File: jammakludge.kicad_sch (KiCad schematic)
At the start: 22 parts, among them J1 Conn_02x28_Odd_Even, J2 Conn_02x28, J3 Conn_02x28

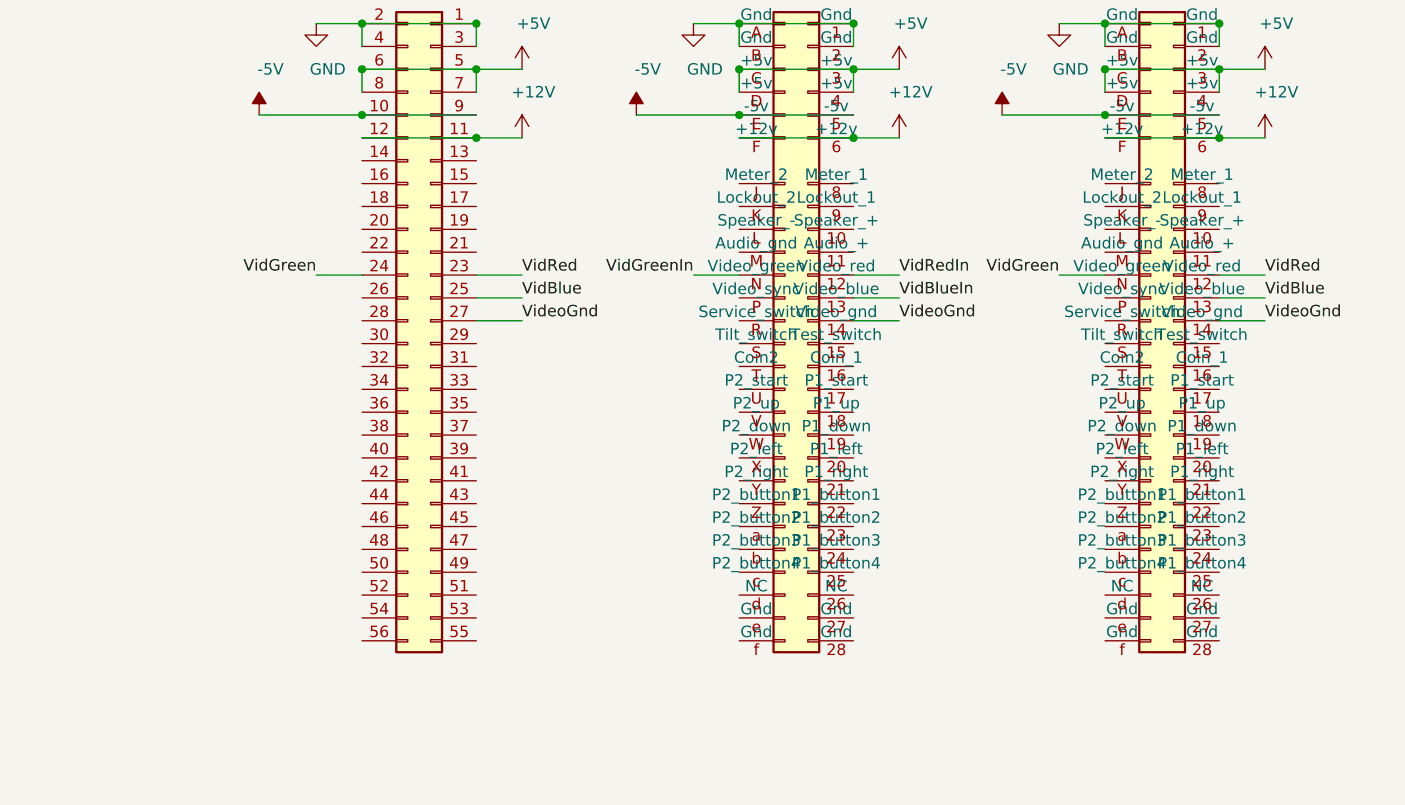
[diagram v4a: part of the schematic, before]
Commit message: labels added
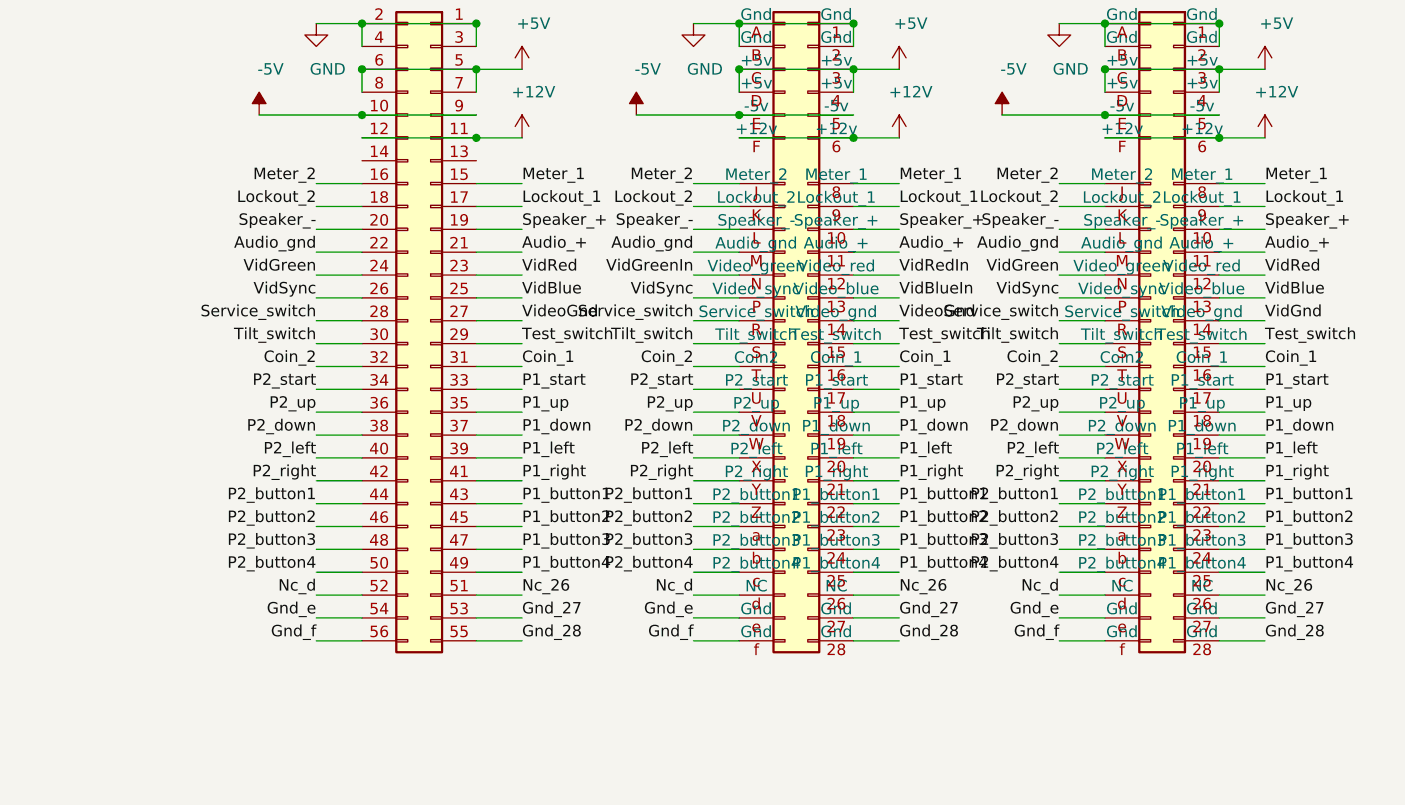
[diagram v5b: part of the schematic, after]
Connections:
- net VideoGnd: no longer J3.14 (Video_gnd)
- net Speaker_+: now reaches J3.10 (Speaker_+)
- net Speaker_+: now also J1.19 (Pin_19), J2.10 (Speaker_+)
- net Audio_+: now reaches J3.11 (Audio_+)
- net Audio_+: now also J1.21 (Pin_21), J2.11 (Audio_+)
- net Test_switch: now reaches J3.15 (Test_switch)
- net Test_switch: now also J1.29 (Pin_29), J2.15 (Test_switch)
- net Coin_1: now reaches J3.16 (Coin_1)
- net Coin_1: now also J1.31 (Pin_31), J2.16 (Coin_1)
- net P1_start: now reaches J3.17 (P1_start)
- net P1_start: now also J1.33 (Pin_33), J2.17 (P1_start)
- net P1_up: now reaches J3.18 (P1_up)
- net P1_up: now also J1.35 (Pin_35), J2.18 (P1_up)
- net P1_down: now reaches J3.19 (P1_down)
- net P1_down: now also J1.37 (Pin_37), J2.19 (P1_down)
- net P1_left: now reaches J3.20 (P1_left)
- net P1_left: now also J1.39 (Pin_39), J2.20 (P1_left)
- net P1_right: now reaches J3.21 (P1_right)
- net P1_right: now also J1.41 (Pin_41), J2.21 (P1_right)
- net P1_button1: now reaches J3.22 (P1_button1)
- net P1_button1: now also J1.43 (Pin_43), J2.22 (P1_button1)
- net P1_button2: now reaches J3.23 (P1_button2)
- net P1_button2: now also J1.45 (Pin_45), J2.23 (P1_button2)
- net P1_button3: now reaches J3.24 (P1_button3)
- net P1_button3: now also J1.47 (Pin_47), J2.24 (P1_button3)
- net P1_button4: now reaches J3.25 (P1_button4)
- net P1_button4: now also J1.49 (Pin_49), J2.25 (P1_button4)
- net Nc_26: now reaches J3.26 (NC)
- net Nc_26: now also J1.51 (Pin_51), J2.26 (NC)
- net Gnd_27: now reaches J3.27 (Gnd)
- net Gnd_27: now also J1.53 (Pin_53), J2.27 (Gnd)
- net Gnd_28: now reaches J3.28 (Gnd)
- net Gnd_28: now also J1.55 (Pin_55), J2.28 (Gnd)
- net Meter_1: now reaches J3.8 (Meter_1)
- net Meter_1: now also J1.15 (Pin_15), J2.8 (Meter_1)
- net Lockout_1: now reaches J3.9 (Lockout_1)
- net Lockout_1: now also J1.17 (Pin_17), J2.9 (Lockout_1)
- net Meter_2: now reaches J3.J (Meter_2)
- net Meter_2: now also J1.16 (Pin_16), J2.J (Meter_2)
- net Lockout_2: now reaches J3.K (Lockout_2)
- net Lockout_2: now also J1.18 (Pin_18), J2.K (Lockout_2)
- net Speaker_-: now reaches J3.L (Speaker_-)
- net Speaker_-: now also J1.20 (Pin_20), J2.L (Speaker_-)
- net Audio_gnd: now reaches J3.M (Audio_gnd)
- net Audio_gnd: now also J1.22 (Pin_22), J2.M (Audio_gnd)
- net VidSync: now reaches J3.P (Video_sync)
- net VidSync: now also J1.26 (Pin_26), J2.P (Video_sync)
- net Service_switch: now reaches J3.R (Service_switch)
- net Service_switch: now also J1.28 (Pin_28), J2.R (Service_switch)
- net Tilt_switch: now reaches J3.S (Tilt_switch)
- net Tilt_switch: now also J1.30 (Pin_30), J2.S (Tilt_switch)
- net Coin_2: now reaches J3.T (Coin2)
- net Coin_2: now also J1.32 (Pin_32), J2.T (Coin2)
- net P2_start: now reaches J3.U (P2_start)
- net P2_start: now also J1.34 (Pin_34), J2.U (P2_start)
- net P2_up: now reaches J3.V (P2_up)
- net P2_up: now also J1.36 (Pin_36), J2.V (P2_up)
- net P2_down: now reaches J3.W (P2_down)
- net P2_down: now also J1.38 (Pin_38), J2.W (P2_down)
- net P2_left: now reaches J3.X (P2_left)
- net P2_left: now also J1.40 (Pin_40), J2.X (P2_left)
- net P2_right: now reaches J3.Y (P2_right)
- net P2_right: now also J1.42 (Pin_42), J2.Y (P2_right)
- net P2_button1: now reaches J3.Z (P2_button1)
- net P2_button1: now also J1.44 (Pin_44), J2.Z (P2_button1)
- net P2_button2: now reaches J3.a (P2_button2)
- net P2_button2: now also J1.46 (Pin_46), J2.a (P2_button2)
- net P2_button3: now reaches J3.b (P2_button3)
- net P2_button3: now also J1.48 (Pin_48), J2.b (P2_button3)
- net P2_button4: now reaches J3.c (P2_button4)
- net P2_button4: now also J1.50 (Pin_50), J2.c (P2_button4)
- net Nc_d: now reaches J3.d (NC)
- net Nc_d: now also J1.52 (Pin_52), J2.d (NC)
- net Gnd_e: now reaches J3.e (Gnd)
- net Gnd_e: now also J1.54 (Pin_54), J2.e (Gnd)
- net Gnd_f: now reaches J3.f (Gnd)
- net Gnd_f: now also J1.56 (Pin_56), J2.f (Gnd)
- new net VidGnd: J3.14 (Video_gnd)

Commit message: Mostly completed layout, fixed some labels that didn't match right. Left to do: better gnd stitching and tidy up
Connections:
- net VideoGnd is gone; now on net VidGnd: J1.27 (Pin_27), J2.14 (Video_gnd)
- net VidBlue: now also J2.13 (Video_blue); no longer J1.25 (Pin_25), J3.13 (Video_blue)
- net VidBlueIn: now also J1.25 (Pin_25), J3.13 (Video_blue); no longer J2.13 (Video_blue)
- net VidGreen: now also J2.N (Video_green); no longer J1.24 (Pin_24), J3.N (Video_green)
- net VidGreenIn: now also J1.24 (Pin_24), J3.N (Video_green); no longer J2.N (Video_green)
- net VidRed: now also J2.12 (Video_red); no longer J1.23 (Pin_23), J3.12 (Video_red)
- net VidRedIn: now also J1.23 (Pin_23), J3.12 (Video_red); no longer J2.12 (Video_red)
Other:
- moved on the sheet: J1, J2
